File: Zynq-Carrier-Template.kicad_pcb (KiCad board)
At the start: 2 copper layers, 49 x 41 mm, 5 parts, among them J1 Zynq_SoM

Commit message: Testing collab functionality
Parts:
- added J3: USB_C_Receptacle_USB2.0_16P, Connector_USB:USB_C_Receptacle_G-Switch_GT-USB-7010ASV, F.Cu at (138.4, 120.1)

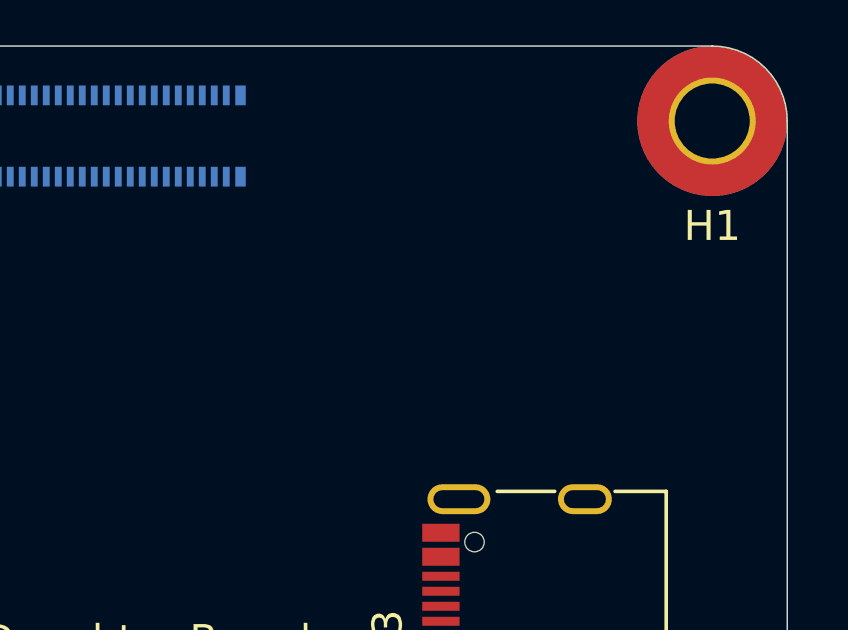
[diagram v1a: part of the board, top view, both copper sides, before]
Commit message: Import BQ25629RYKR
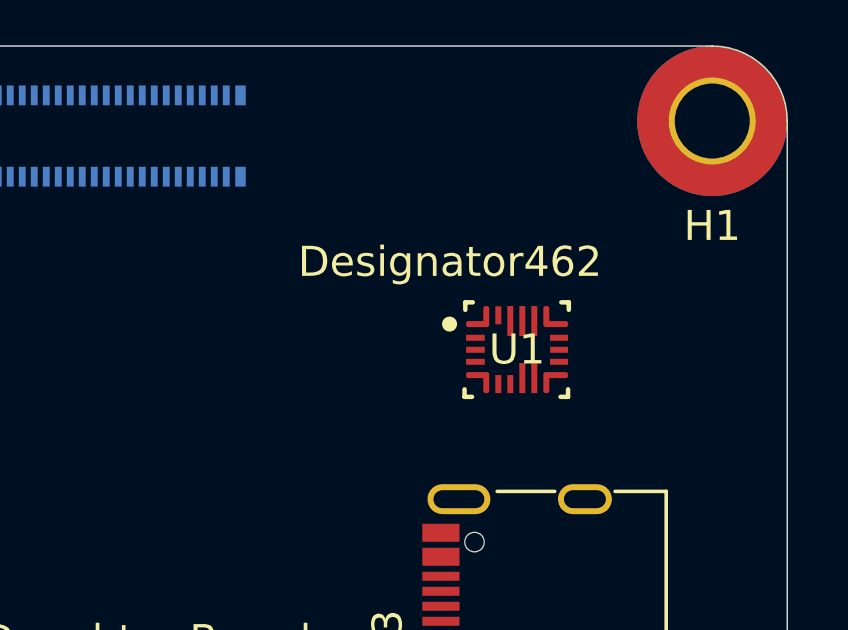
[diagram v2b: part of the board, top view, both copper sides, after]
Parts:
- added U1: BQ25629RYKR, BQ25629RYKR:RYK0018A-MFG, F.Cu at (137.2, 110.8)

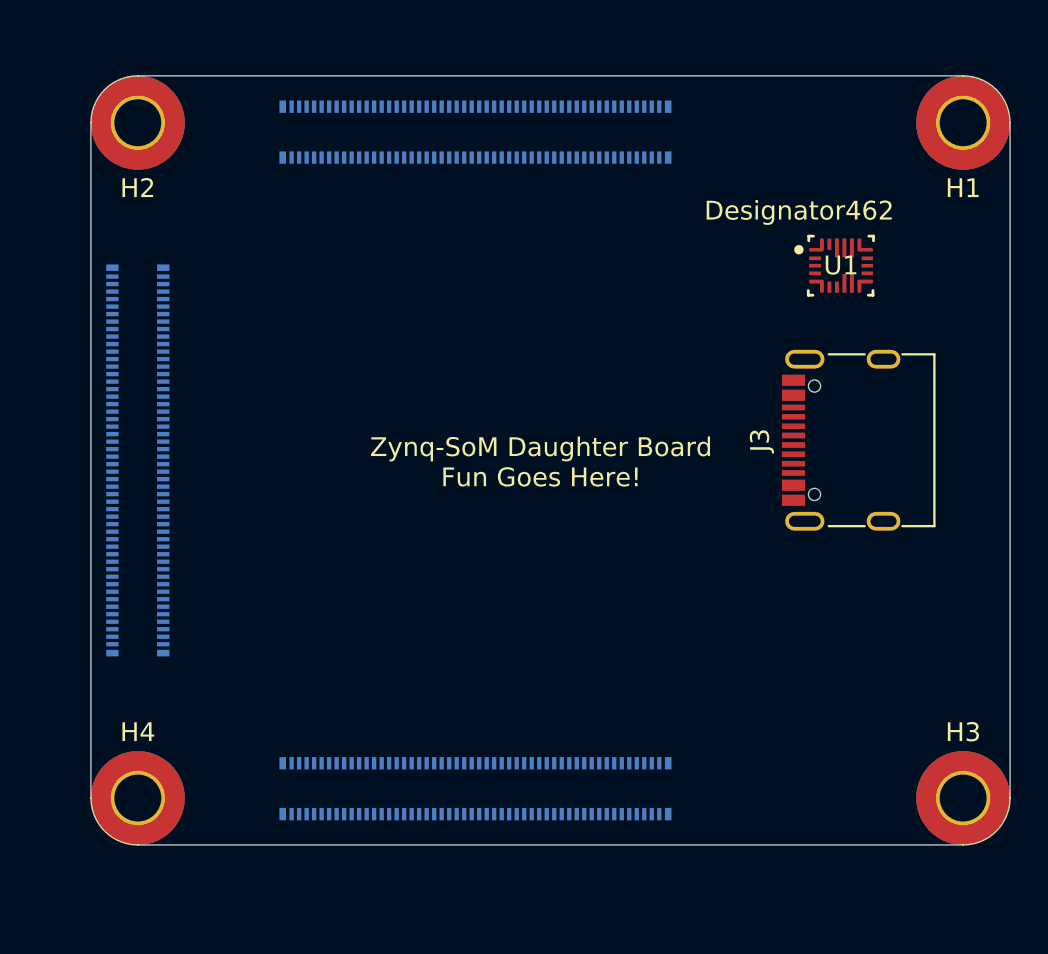
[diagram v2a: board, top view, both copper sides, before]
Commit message: Copper Fill demo
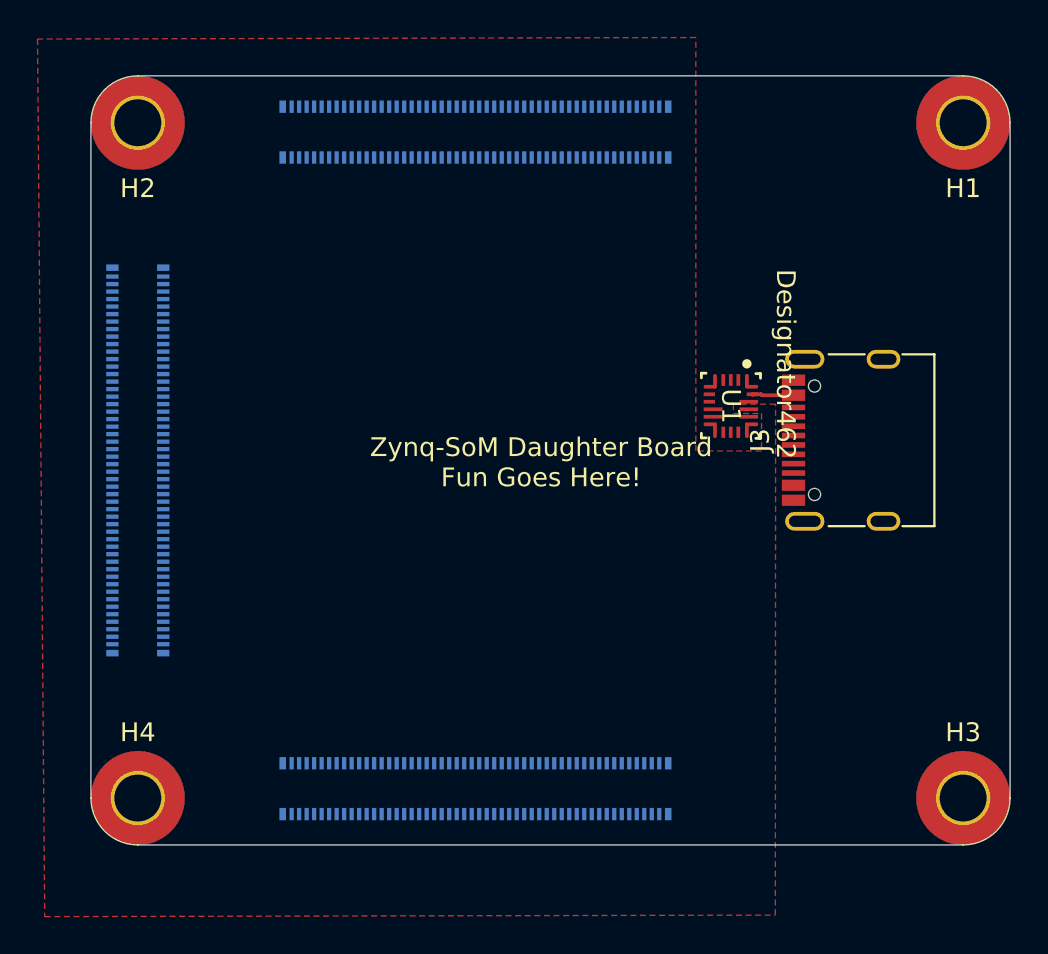
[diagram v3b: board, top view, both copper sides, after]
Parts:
- moved U1 9.51 mm to (131.3, 118.2), turned to -90 degrees
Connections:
- J3 pad A1: Net-(J3-GND-PadA1) -> GND
- J3 pad A12: Net-(J3-GND-PadA1) -> GND
- J3 pad A4: Net-(J3-VBUS-PadA4) -> /VBUS
- J3 pad A9: Net-(J3-VBUS-PadA4) -> /VBUS
- J3 pad B1: Net-(J3-GND-PadA1) -> GND
- J3 pad B12: Net-(J3-GND-PadA1) -> GND
- J3 pad B4: Net-(J3-VBUS-PadA4) -> /VBUS
- J3 pad B9: Net-(J3-VBUS-PadA4) -> /VBUS
- U1 pad 15: unconnected-(U1-GND-Pad15) -> GND
- U1 pad 16: unconnected-(U1-SW-Pad16) -> +5V
- U1 pad 18: unconnected-(U1-VBUS-Pad18) -> /VBUS
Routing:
- net /VBUS: track 0.00 -> 2.24 mm
- added copper zone on F.Cu, net +5V
